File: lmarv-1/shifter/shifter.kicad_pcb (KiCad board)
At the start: 4 copper layers, 205 x 113.6 mm, 138 parts, among them J1 Conn_02x09_Odd_Even, P1 dual-pcie-cardedge, U1 74LVC541, U10 74LVC541, U11 74LVC541, U12 74LVC541, U13 74LVC541, U14 74LVC541, U15 74LVC541, U16 74LVC541, U17 74LVC541, U18 74LVC541, U19 74LVC541, U2 74LVC04, U20 74LVC541, U21 74LVC541, U22 74LVC541, U23 74LVC541, U24 74LVC541, U25 74LVC541, U26 74LVC541, U27 74LVC541, U28 74LVC541, U29 74LVC541, U3 74LVC08, U30 74LVC541, U31 74LVC541, U32 74LVC541, U33 74LVC541, U34 74LVC541, U35 74LVC541, U36 74LVC541, U37 74LVC541, U38 74LVC541, U39 74LVC541, U4 74LVC32, U40 74LVC541, U41 74LVC541, U42 74LVC541, U43 74LVC541, U44 74LVC541, U45 74LVC541, U46 74LVC541, U47 74LVC541, U48 74LVC541, U49 74LVC541, U5 74LVC541, U50 74LVC541, U51 74LVC541, U52 74LVC541, U53 74LVC541, U54 74LVC541, U55 74LVC541, U56 74LVC541, U57 74LVC541, U58 74LVC541, U59 74LVC541, U6 74LVC541, U60 74LVC541, U61 74LVC541, U62 74LVC541, U63 74LVC541, U64 74LVC541, U7 74LVC541, U8 74LVC541, U9 74LVC541

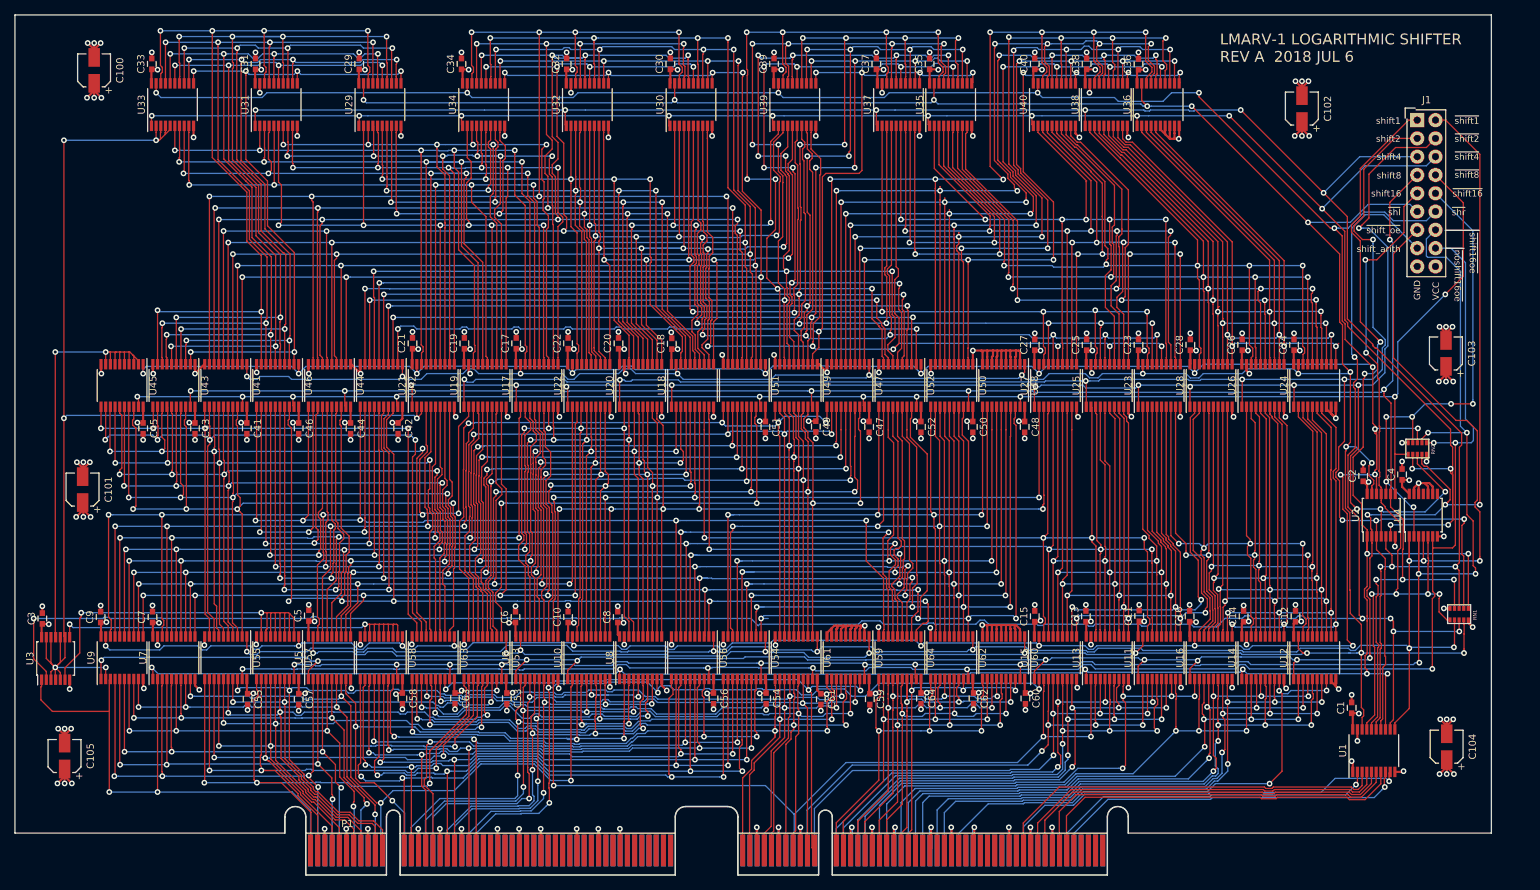
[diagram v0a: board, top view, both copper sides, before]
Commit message: Adds tinyfpga test things
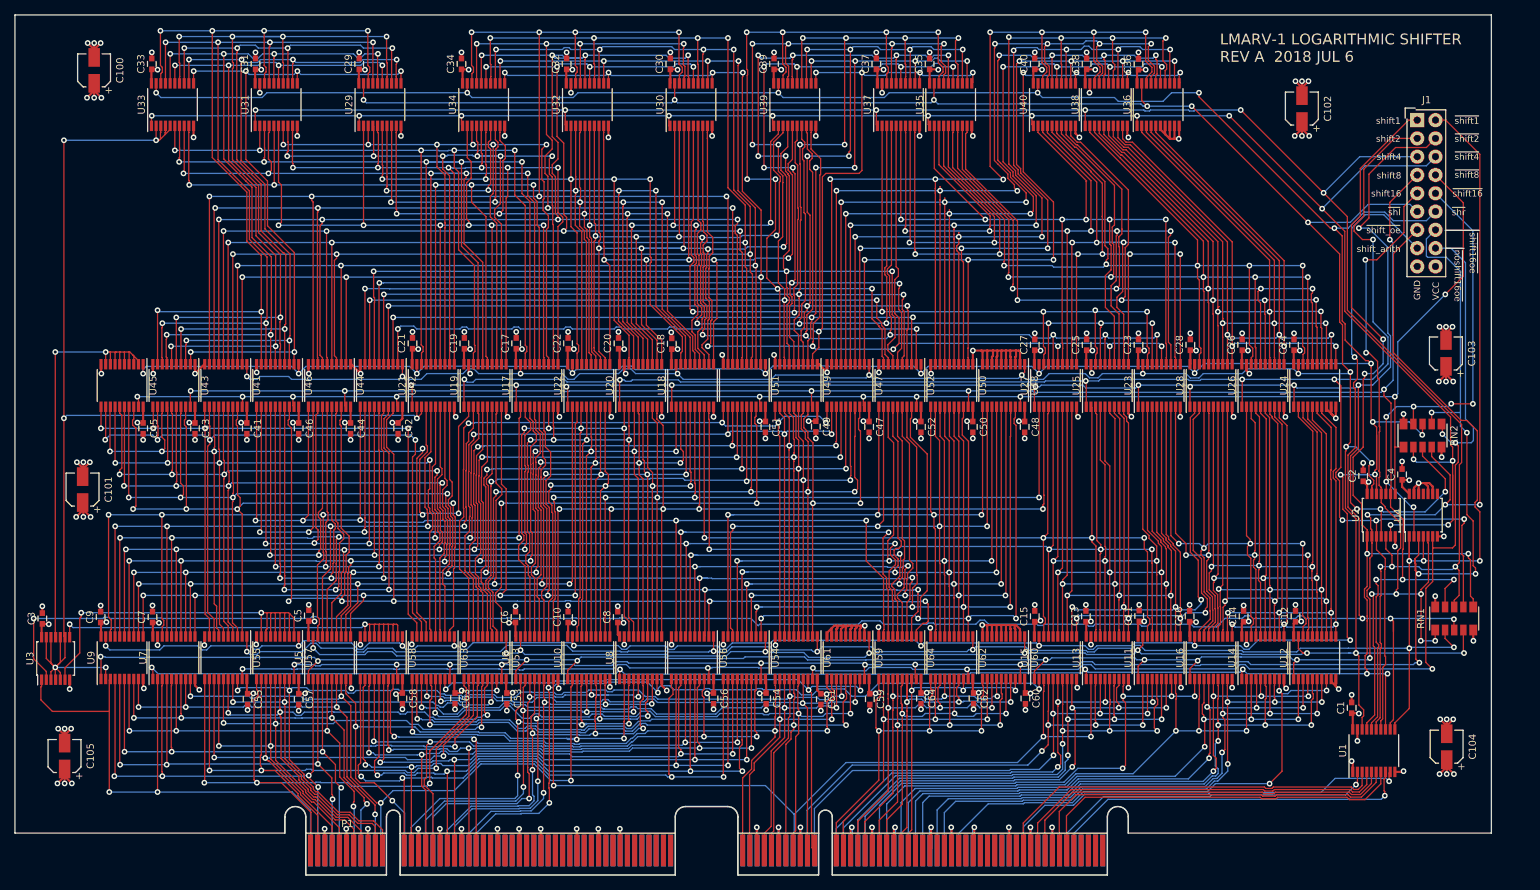
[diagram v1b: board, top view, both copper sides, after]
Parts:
- RN1, RN2: footprint lmarv:YC158 -> lmarv:Yageo_YC358
- moved RN2 1.94 mm to (260.4, 105.4)
- moved RN1 0.91 mm to (264.8, 130.8)
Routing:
- net /~shift_16_oe: track 264.6 -> 260.6 mm
- net /shift16: track 103.4 -> 107.0 mm, vias 6 -> 7
- net /~shift_left: track 608.2 -> 606.0 mm
- net VCC: track 279.9 -> 281.8 mm
- net /s8[4]: track 128.2 -> 126.6 mm
- net /~shift2: track 244.8 -> 246.1 mm
- net /s2[11]: track 144.9 -> 143.7 mm
- net /~shift16: track 67.9 -> 66.7 mm
- net /s8[0]: track 132.6 -> 131.6 mm
- net /~shift4: track 274.2 -> 273.2 mm
- net /~shift_oe: track 282.3 -> 281.4 mm
- net /shift_arith': track 50.4 -> 51.1 mm
- net /~shift1: track 304.9 -> 305.5 mm
- net /~shift8: track 237.8 -> 237.2 mm
- net /~noshift_16_oe: track 246.4 -> 247.0 mm
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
